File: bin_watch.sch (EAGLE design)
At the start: 92 parts, among them IC1 MEGA48/88/168-MU, J1 USB3100-XX-X_REVB, Q1 32.768kHz, T1 2N7002BKV, T2 2N7002BKV, T3 2N7002BKV, T4 2N7002BKV, T5 PMDT670UPE, T6 PMDT670UPE, T7 PMDT670UPE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

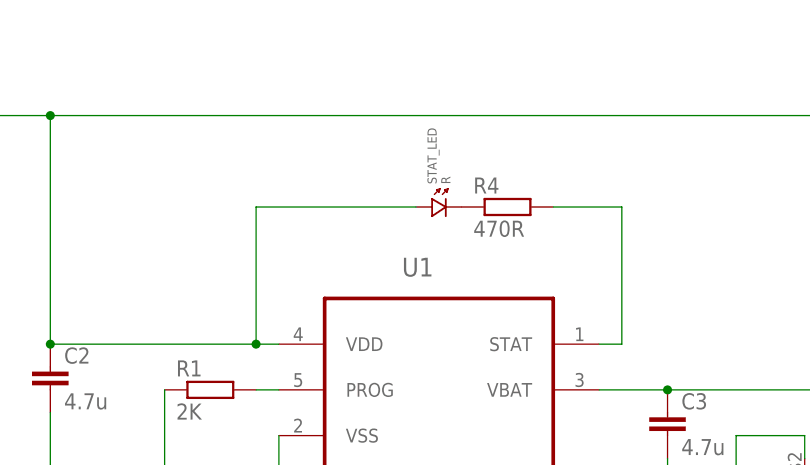
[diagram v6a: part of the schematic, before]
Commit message: Board shrunk
Sized down version
TODO: Power supply routing
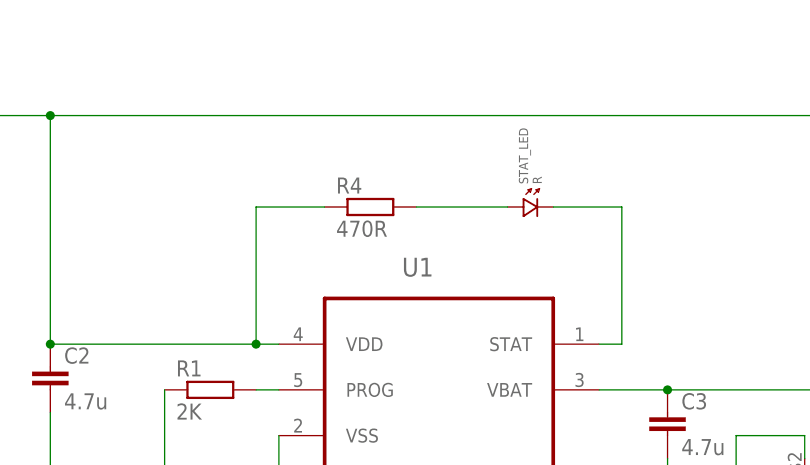
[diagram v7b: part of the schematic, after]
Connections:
- removed net N$3: R4.1, STAT_LED.2
- new net STAT_R: R4.2, STAT_LED.1
- net STAT: now also STAT_LED.2; no longer R4.2
- net VBUS: now also R4.1; no longer STAT_LED.1
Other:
- moved on the sheet: R4, STAT_LED
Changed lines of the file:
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@@
 <instance part="R1" gate="G$1" x="104.14" y="246.38"/>
 <instance part="SUPPLY19" gate="GND" x="99.06" y="223.52"/>
-<instance part="STAT_LED" gate="G$1" x="129.54" y="266.7"/>
-<instance part="R4" gate="G$1" x="137.16" y="266.7"/>
+<instance part="STAT_LED" gate="G$1" x="139.7" y="266.7"/>
+<instance part="R4" gate="G$1" x="121.92" y="266.7"/>
 <instance part="C3" gate="G$1" x="154.94" y="243.84"/>
 <instance part="SUPPLY20" gate="GND" x="154.94" y="223.52"/>
@@
 </busses>
 <nets>
-<net name="XTAL_P" class="0">
+<net name="XTAL_P" class="4">
 <segment>
 <wire x1="-7.62" y1="78.74" x2="-7.62" y2="22.86" width="0.1524" layer="91"/>
@@
 </segment>
 </net>
-<net name="XTAL_N" class="0">
+<net name="XTAL_N" class="4">
 <segment>
 <pinref part="Q1" gate="G$1" pin="2"/>
@@
 <wire x1="109.22" y1="251.46" x2="111.76" y2="251.46" width="0.1524" layer="91"/>
 <wire x1="109.22" y1="251.46" x2="109.22" y2="266.7" width="0.1524" layer="91"/>
+<wire x1="109.22" y1="266.7" x2="116.84" y2="266.7" width="0.1524" layer="91"/>
 <junction x="109.22" y="251.46"/>
-<pinref part="STAT_LED" gate="G$1" pin="1"/>
-<wire x1="109.22" y1="266.7" x2="127" y2="266.7" width="0.1524" layer="91"/>
 <pinref part="C2" gate="G$1" pin="1"/>
 <junction x="86.36" y="251.46"/>
@@
 <junction x="210.82" y="276.86"/>
 <junction x="86.36" y="276.86"/>
+<pinref part="R4" gate="G$1" pin="1"/>
 </segment>
 </net>
@@
 </segment>
 </net>
-<net name="N$3" class="0">
-<segment>
-<pinref part="STAT_LED" gate="G$1" pin="2"/>
-<pinref part="R4" gate="G$1" pin="1"/>
-</segment>
-</net>
 <net name="STAT" class="0">
 <segment>
-<pinref part="R4" gate="G$1" pin="2"/>
 <wire x1="142.24" y1="266.7" x2="149.86" y2="266.7" width="0.1524" layer="91"/>
 <wire x1="149.86" y1="266.7" x2="149.86" y2="251.46" width="0.1524" layer="91"/>
 <pinref part="U1" gate="A" pin="STAT"/>
 <wire x1="149.86" y1="251.46" x2="147.32" y2="251.46" width="0.1524" layer="91"/>
+<pinref part="STAT_LED" gate="G$1" pin="2"/>
 </segment>
 </net>
@@
 </segment>
 </net>
+<net name="STAT_R" class="0">
+<segment>
+<pinref part="STAT_LED" gate="G$1" pin="1"/>
+<pinref part="R4" gate="G$1" pin="2"/>
+<wire x1="127" y1="266.7" x2="137.16" y2="266.7" width="0.1524" layer="91"/>
+</segment>
+</net>

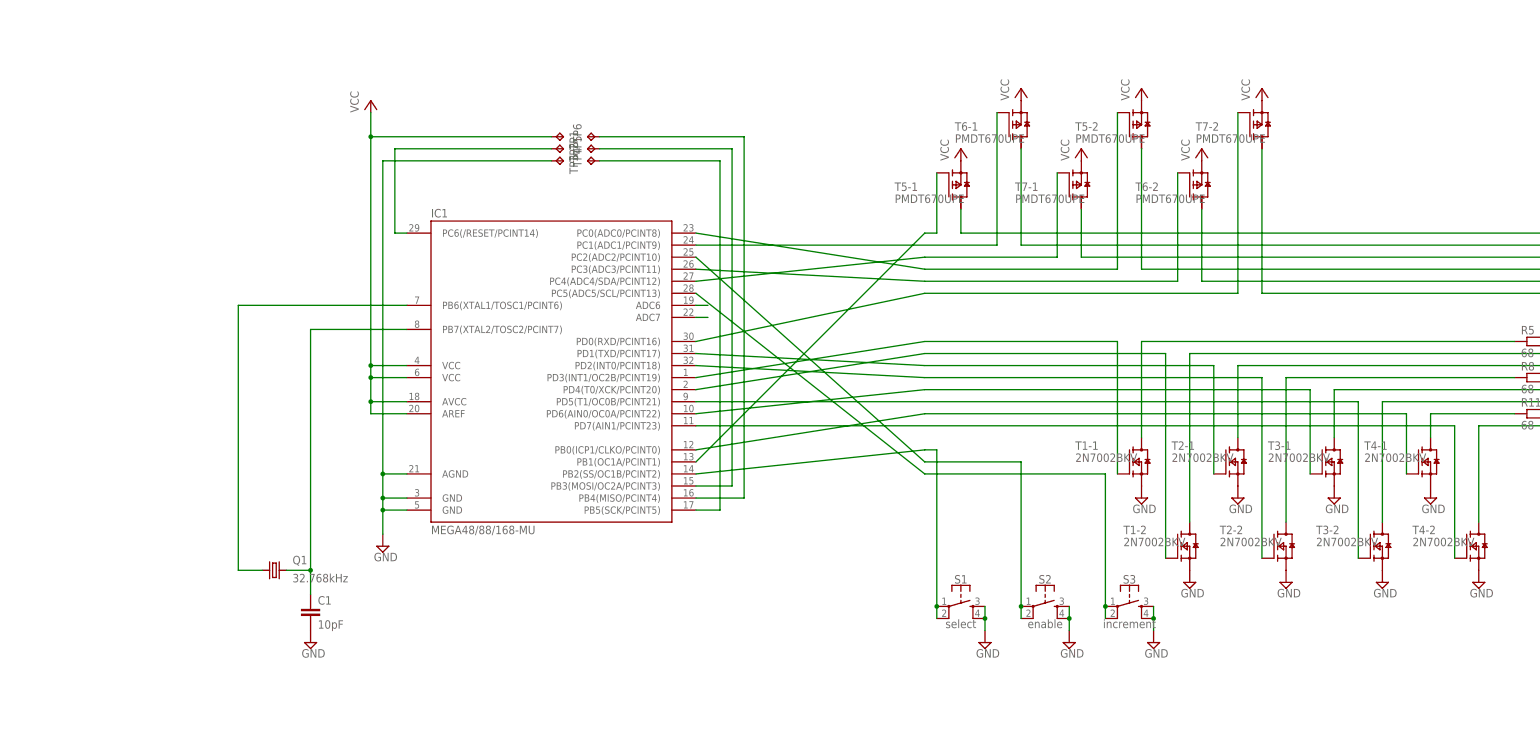
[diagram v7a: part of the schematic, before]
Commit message: Added pull resistors to N-channels
This way, when the gates are not driven, they default to OFF
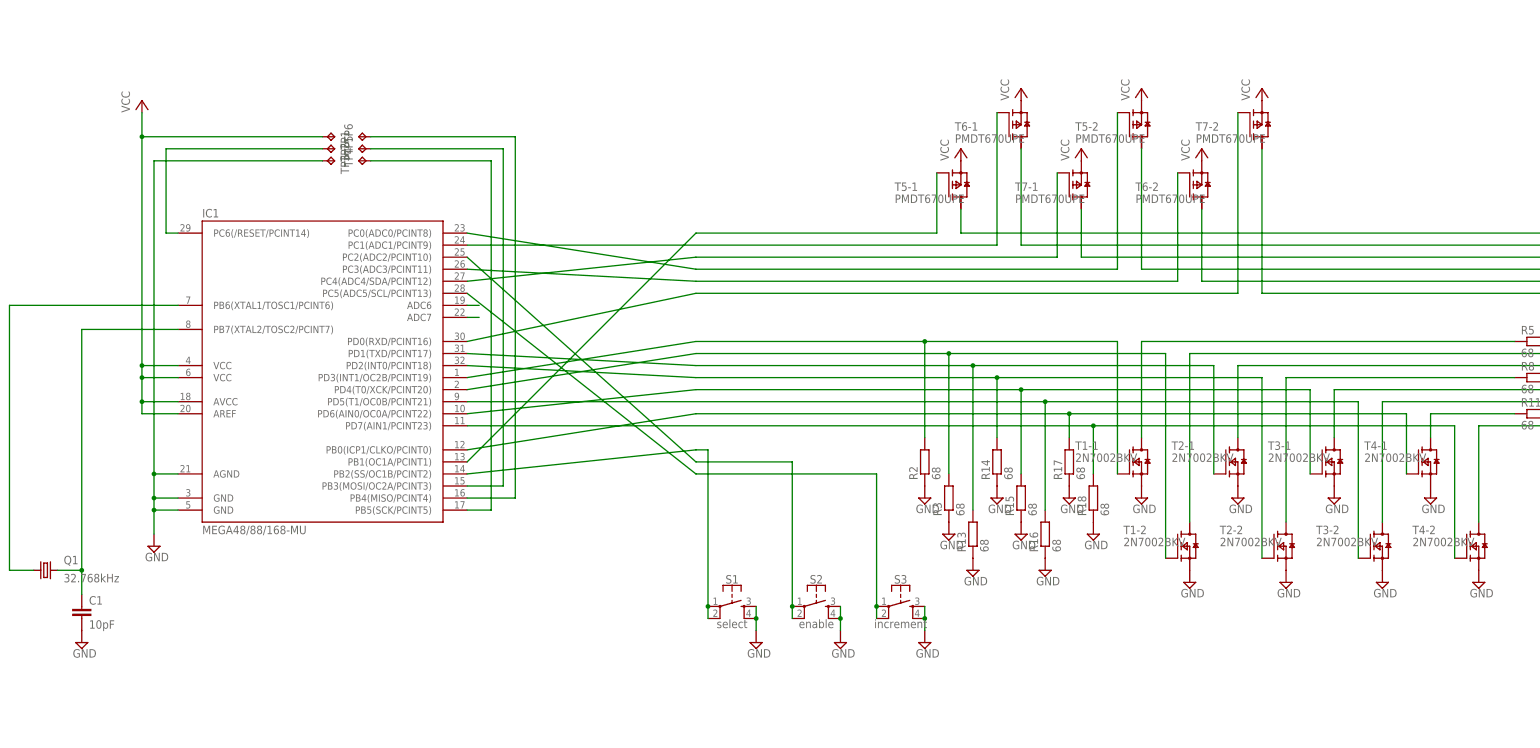
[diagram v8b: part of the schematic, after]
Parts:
- added R13, R14, R15, R16, R17, R18, R2, R3: 68, rcl:R-EU_R0603
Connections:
- net GND: now also R13.1, R14.1, R15.1, R16.1, R17.1, R18.1, R2.1, R3.1
- net PD0: now also R2.2
- net PD1: now also R3.2
- net PD2: now also R13.2
- net PD3: now also R14.2
- net PD4: now also R15.2
- net PD5: now also R16.2
- net PD6: now also R17.2
- net PD7: now also R18.2
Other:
- moved on the sheet: C1, IC1, Q1, S1, S2, S3, TP1, TP2, TP3, TP4, TP5, TP6
